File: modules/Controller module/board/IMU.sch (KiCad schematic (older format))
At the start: 9 parts, among them J8 Conn_01x08_Female, U4 MPU-6050

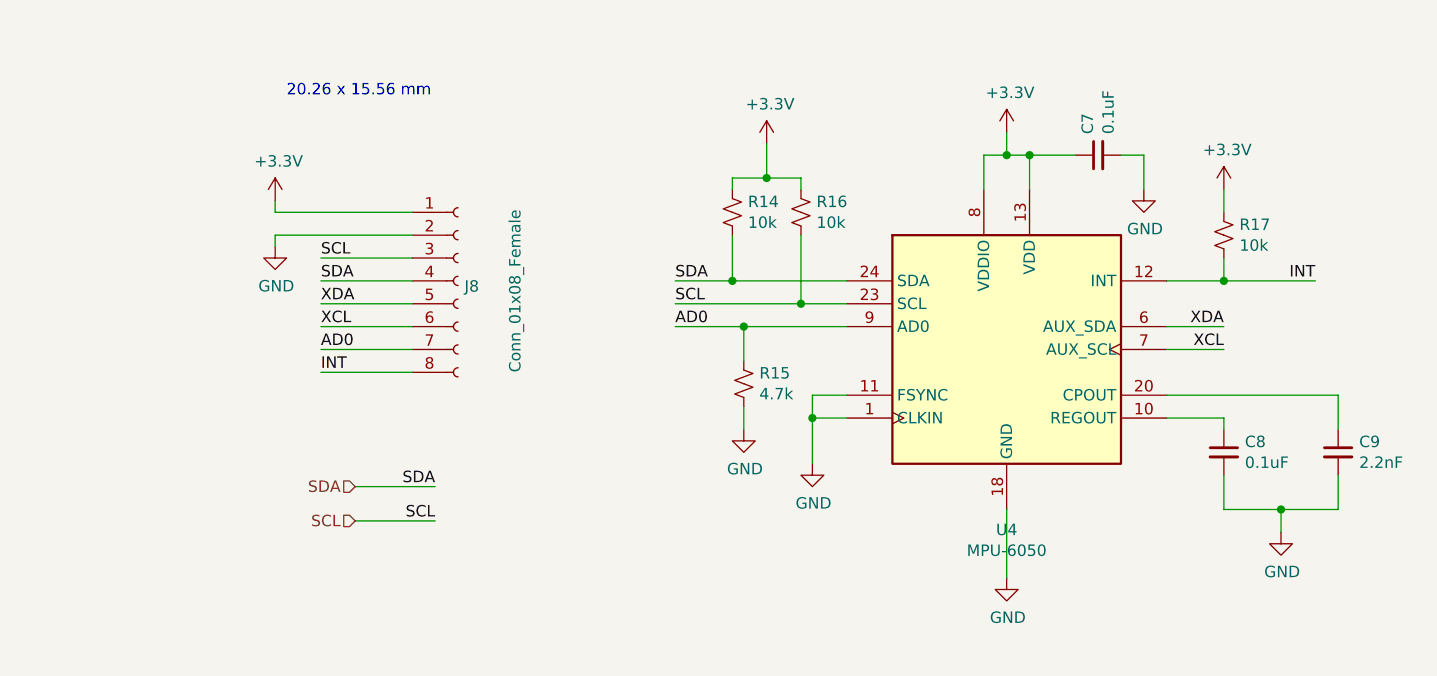
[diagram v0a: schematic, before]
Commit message: Controller module: Schematic and PCB layout
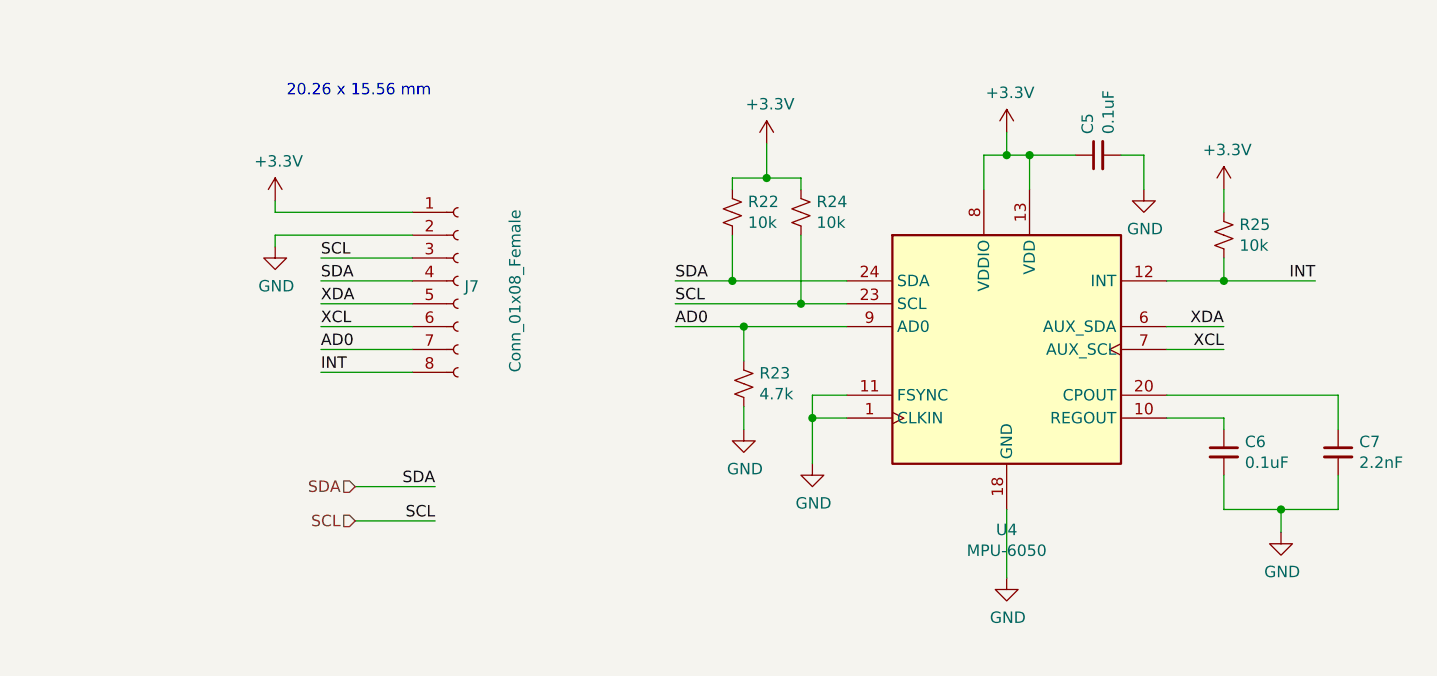
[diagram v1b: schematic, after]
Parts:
- J7: renamed from J8; footprint Connector_PinSocket_2.54mm:PinSocket_1x08_P2.54mm_Vertical -> Board:MPU6050_Breakout
- renumbered C7 to C5, C8 to C6, C9 to C7, R14 to R22, R15 to R23, R16 to R24, R17 to R25
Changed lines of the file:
@@
 $EndDescr
 $Comp
-L Device:R_Small_US R14
+L Device:R_Small_US R22
 U 1 1 61A150D2
 P 5950 2800
-F 0 "R14" H 6018 2846 50  0000 L CNN
+F 0 "R22" H 6018 2846 50  0000 L CNN
 F 1 "10k" H 6018 2755 50  0000 L CNN
 F 2 "Resistor_SMD:R_0805_2012Metric_Pad1.20x1.40mm_HandSolder" H 5950 2800 50  0001 C CNN
@@
 $EndComp
 $Comp
-L Device:R_Small_US R16
+L Device:R_Small_US R24
 U 1 1 61A15DBA
 P 6250 2800
-F 0 "R16" H 6318 2846 50  0000 L CNN
+F 0 "R24" H 6318 2846 50  0000 L CNN
 F 1 "10k" H 6318 2755 50  0000 L CNN
 F 2 "Resistor_SMD:R_0805_2012Metric_Pad1.20x1.40mm_HandSolder" H 6250 2800 50  0001 C CNN
@@
 	6300 3600 6300 3700
 $Comp
-L power:GND #PWR044
+L power:GND #PWR047
 U 1 1 61A173F2
 P 7150 4400
-F 0 "#PWR044" H 7150 4150 50  0001 C CNN
+F 0 "#PWR047" H 7150 4150 50  0001 C CNN
 F 1 "GND" H 7155 4227 50  0000 C CNN
 F 2 "" H 7150 4400 50  0001 C CNN
@@
 	7150 4400 7150 4100
 $Comp
-L Device:C_Small C9
+L Device:C_Small C7
 U 1 1 61A181FF
 P 8600 3850
-F 0 "C9" H 8692 3896 50  0000 L CNN
+F 0 "C7" H 8692 3896 50  0000 L CNN
 F 1 "2.2nF" H 8692 3805 50  0000 L CNN
 F 2 "Capacitor_SMD:C_0805_2012Metric_Pad1.18x1.45mm_HandSolder" H 8600 3850 50  0001 C CNN
@@
 $EndComp
 $Comp
-L Device:C_Small C8
+L Device:C_Small C6
 U 1 1 61A18A43
 P 8100 3850
-F 0 "C8" H 8192 3896 50  0000 L CNN
+F 0 "C6" H 8192 3896 50  0000 L CNN
 F 1 "0.1uF" H 8192 3805 50  0000 L CNN
 F 2 "Capacitor_SMD:C_0805_2012Metric_Pad1.18x1.45mm_HandSolder" H 8100 3850 50  0001 C CNN
@@
 	8350 4100 8600 4100
 $Comp
-L power:GND #PWR040
+L power:GND #PWR043
 U 1 1 61A1AE2E
 P 6000 3750
-F 0 "#PWR040" H 6000 3500 50  0001 C CNN
+F 0 "#PWR043" H 6000 3500 50  0001 C CNN
 F 1 "GND" H 6005 3577 50  0000 C CNN
 F 2 "" H 6000 3750 50  0001 C CNN
@@
 $EndComp
 $Comp
-L power:GND #PWR047
+L power:GND #PWR050
 U 1 1 61A1B162
 P 8350 4200
-F 0 "#PWR047" H 8350 3950 50  0001 C CNN
+F 0 "#PWR050" H 8350 3950 50  0001 C CNN
 F 1 "GND" H 8355 4027 50  0000 C CNN
 F 2 "" H 8350 4200 50  0001 C CNN
@@
 INT
 $Comp
-L power:+3.3V #PWR041
+L power:+3.3V #PWR044
 U 1 1 61A1F691
 P 6100 2500
-F 0 "#PWR041" H 6100 2350 50  0001 C CNN
+F 0 "#PWR044" H 6100 2350 50  0001 C CNN
 F 1 "+3.3V" H 6115 2673 50  0000 C CNN
 F 2 "" H 6100 2500 50  0001 C CNN
@@
 	6000 3300 6450 3300
 $Comp
-L Device:R_Small_US R15
+L Device:R_Small_US R23
 U 1 1 61A2410C
 P 6000 3550
-F 0 "R15" H 6068 3596 50  0000 L CNN
+F 0 "R23" H 6068 3596 50  0000 L CNN
 F 1 "4.7k" H 6068 3505 50  0000 L CNN
 F 2 "Resistor_SMD:R_0805_2012Metric_Pad1.20x1.40mm_HandSolder" H 6000 3550 50  0001 C CNN
@@
 AD0
 $Comp
-L Device:R_Small_US R17
+L Device:R_Small_US R25
 U 1 1 61A254F5
 P 8100 2900
-F 0 "R17" H 8168 2946 50  0000 L CNN
+F 0 "R25" H 8168 2946 50  0000 L CNN
 F 1 "10k" H 8168 2855 50  0000 L CNN
 F 2 "Resistor_SMD:R_0805_2012Metric_Pad1.20x1.40mm_HandSolder" H 8100 2900 50  0001 C CNN
@@
 $EndComp
 $Comp
-L power:+3.3V #PWR046
+L power:+3.3V #PWR049
 U 1 1 61A254FC
 P 8100 2700
-F 0 "#PWR046" H 8100 2550 50  0001 C CNN
+F 0 "#PWR049" H 8100 2550 50  0001 C CNN
 F 1 "+3.3V" H 8115 2873 50  0000 C CNN
 F 2 "" H 8100 2700 50  0001 C CNN
@@
 	8100 2700 8100 2800
 $Comp
-L power:GND #PWR042
+L power:GND #PWR045
 U 1 1 61A2C29B
 P 6300 3900
-F 0 "#PWR042" H 6300 3650 50  0001 C CNN
+F 0 "#PWR045" H 6300 3650 50  0001 C CNN
 F 1 "GND" H 6305 3727 50  0000 C CNN
 F 2 "" H 6300 3900 50  0001 C CNN
@@
 AD0
 $Comp
-L Connector:Conn_01x08_Female J8
+L Connector:Conn_01x08_Female J7
 U 1 1 61A32798
 P 4750 3100
-F 0 "J8" H 4778 3076 50  0000 L CNN
+F 0 "J7" H 4778 3076 50  0000 L CNN
 F 1 "Conn_01x08_Female" V 5000 2700 50  0000 L CNN
-F 2 "Connector_PinSocket_2.54mm:PinSocket_1x08_P2.54mm_Vertical" H 4750 3100 50  0001 C CNN
+F 2 "Board:MPU6050_Breakout" H 4750 3100 50  0001 C CNN
 F 3 "~" H 4750 3100 50  0001 C CNN
 	1    4750 3100
@@
 	3950 2900 3950 2950
 $Comp
-L power:+3.3V #PWR038
+L power:+3.3V #PWR041
 U 1 1 61A36F21
 P 3950 2750
-F 0 "#PWR038" H 3950 2600 50  0001 C CNN
+F 0 "#PWR041" H 3950 2600 50  0001 C CNN
 F 1 "+3.3V" H 3965 2923 50  0000 C CNN
 F 2 "" H 3950 2750 50  0001 C CNN
@@
 $EndComp
 $Comp
-L power:GND #PWR039
+L power:GND #PWR042
 U 1 1 61A37647
 P 3950 2950
-F 0 "#PWR039" H 3950 2700 50  0001 C CNN
+F 0 "#PWR042" H 3950 2700 50  0001 C CNN
 F 1 "GND" H 3955 2777 50  0000 C CNN
 F 2 "" H 3950 2950 50  0001 C CNN
@@
 20.26 x 15.56 mm
 $Comp
-L power:+3.3V #PWR043
+L power:+3.3V #PWR046
 U 1 1 61A16C94
 P 7150 2450
-F 0 "#PWR043" H 7150 2300 50  0001 C CNN
+F 0 "#PWR046" H 7150 2300 50  0001 C CNN
 F 1 "+3.3V" H 7165 2623 50  0000 C CNN
 F 2 "" H 7150 2450 50  0001 C CNN
@@
 $EndComp
 $Comp
-L Device:C_Small C7
+L Device:C_Small C5
 U 1 1 61A3D7BC
 P 7550 2550
-F 0 "C7" H 7642 2596 50  0000 L CNN
+F 0 "C5" H 7642 2596 50  0000 L CNN
 F 1 "0.1uF" H 7642 2505 50  0000 L CNN
 F 2 "Capacitor_SMD:C_0805_2012Metric_Pad1.18x1.45mm_HandSolder" H 7550 2550 50  0001 C CNN
@@
 	6000 3650 6000 3750
 $Comp
-L power:GND #PWR045
+L power:GND #PWR048
 U 1 1 61A3EAA3
 P 7750 2700
-F 0 "#PWR045" H 7750 2450 50  0001 C CNN
+F 0 "#PWR048" H 7750 2450 50  0001 C CNN
 F 1 "GND" H 7755 2527 50  0000 C CNN
 F 2 "" H 7750 2700 50  0001 C CNN

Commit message: Controller module: PCB complete
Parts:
- renumbered R22 to R23, R23 to R24, R24 to R25, R25 to R26
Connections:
- net +3V3: no longer J7.1 (Pin_1)
- new net VCC: J7.1 (Pin_1)
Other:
- moved on the sheet: C5, C6, C7, J7, R23, R24, R25, R26, U4

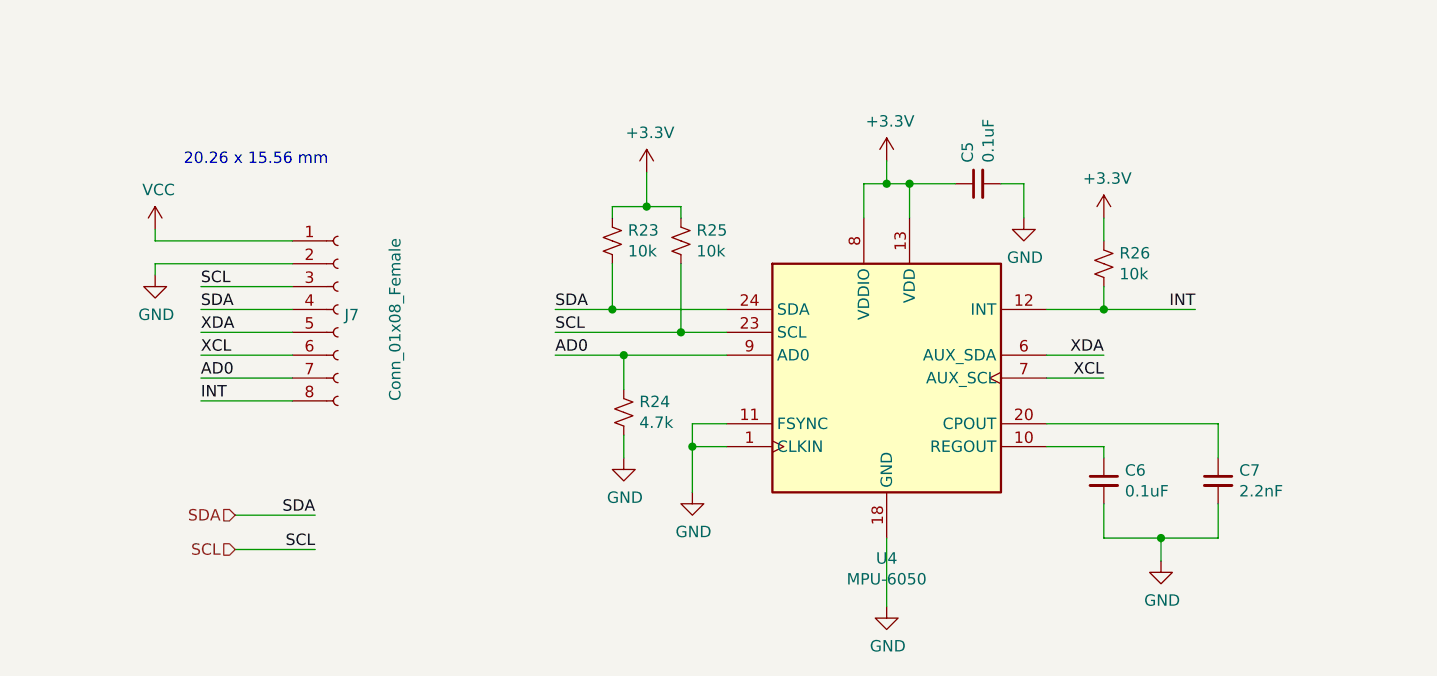
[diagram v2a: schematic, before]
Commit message: PCB: IMU
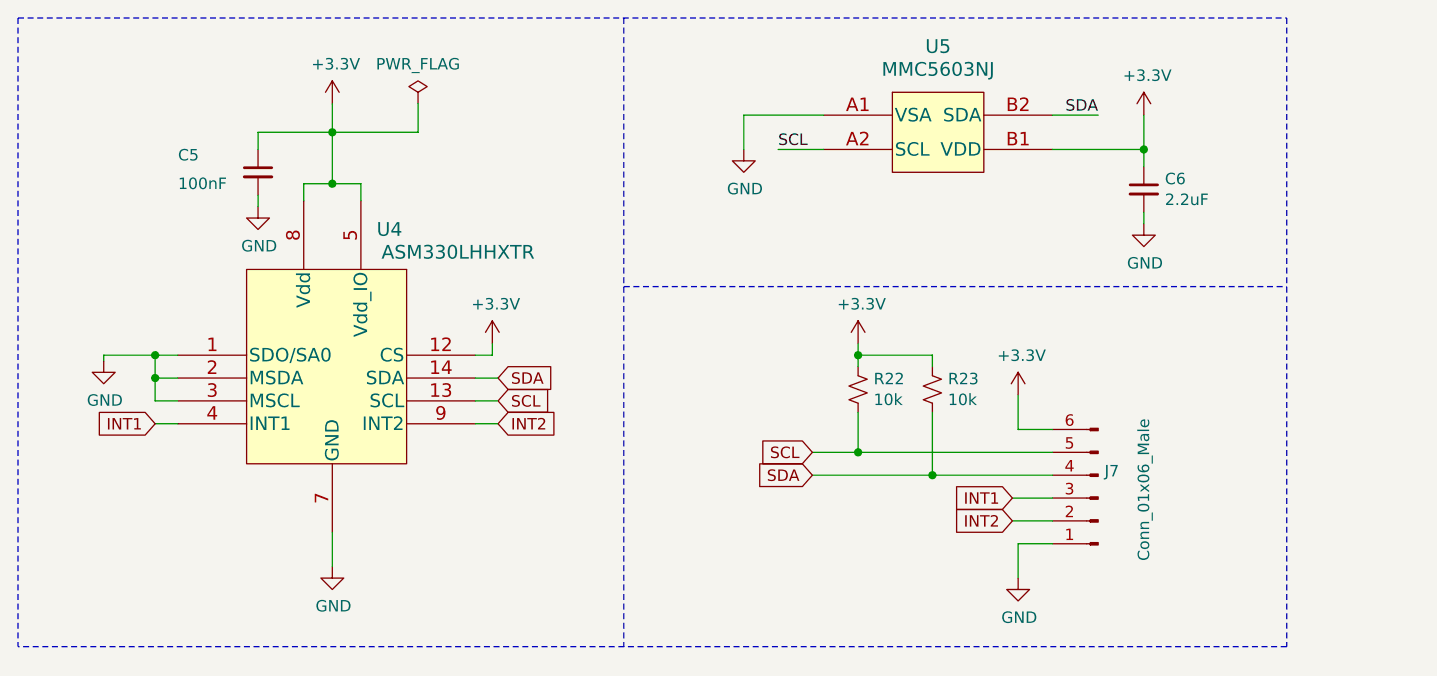
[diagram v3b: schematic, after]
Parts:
- removed C7: 2.2nF, Capacitor_SMD:C_0805_2012Metric_Pad1.18x1.45mm_HandSolder, symbol Device:C_Small
- removed J7: Conn_01x08_Female, Board:MPU6050_Breakout, symbol Connector:Conn_01x08_Female
- removed R24: 4.7k, Resistor_SMD:R_0805_2012Metric_Pad1.20x1.40mm_HandSolder, symbol Device:R_Small_US
- removed R25, R26: 10k, Resistor_SMD:R_0805_2012Metric_Pad1.20x1.40mm_HandSolder, symbol Device:R_Small_US
- removed U4: MPU-6050, Sensor_Motion:InvenSense_QFN-24_4x4mm_P0.5mm, symbol Sensor_Motion:MPU-6050
- added J7: Conn_01x06_Male, Board:SolderWire_1x06_P2.54mm, symbol Connector:Conn_01x06_Male
- added R22: 10k, Resistor_SMD:R_0603_1608Metric_Pad0.98x0.95mm_HandSolder, symbol Device:R_Small_US
- added U4: ASM330LHHXTR, Board:ASM330LHHXTR, symbol ASM330LHHXTR:ASM330LHHXTR
- added U5: MMC5603NJ, Board:MMC5603NJ, symbol MMC5603NJ:MMC5603NJ
- C5: value 0.1uF -> 100nF; footprint Capacitor_SMD:C_0805_2012Metric_Pad1.18x1.45mm_HandSolder -> Capacitor_SMD:C_0603_1608Metric_Pad1.08x0.95mm_HandSolder
- C6: value 0.1uF -> 2.2uF; footprint Capacitor_SMD:C_0805_2012Metric_Pad1.18x1.45mm_HandSolder -> Capacitor_SMD:C_0603_1608Metric_Pad1.08x0.95mm_HandSolder
- R23: footprint Resistor_SMD:R_0805_2012Metric_Pad1.20x1.40mm_HandSolder -> Resistor_SMD:R_0603_1608Metric_Pad0.98x0.95mm_HandSolder
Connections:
- net +3V3: now also C6.1, J7.6 (Pin_6), R22.1, U4.12 (CS), U4.5 (Vdd_IO), U4.8 (Vdd), U5.B1 (VDD)
- net GND: now also J7.1 (Pin_1), U4.1 (SDO/SA0), U4.2 (MSDA), U4.3 (MSCL), U4.7 (GND), U5.A1 (VSA)
- net SCL: now also J7.5 (Pin_5), R22.2, U4.13 (SCL), U5.A2 (SCL)
- net SDA: now also J7.4 (Pin_4), U4.14 (SDA), U5.B2 (SDA)
- new net INT1: J7.3 (Pin_3), U4.4 (INT1)
- new net INT2: J7.2 (Pin_2), U4.9 (INT2)
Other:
- note removed: "20.26 x 15.56 mm"

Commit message: Controller module: Optical Flow Sensor Connector
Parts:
- renumbered C5 to C4, C6 to C5, J7 to J6, R22 to R20, R23 to R21
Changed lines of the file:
@@
 $Descr A4 11693 8268
 encoding utf-8
-Sheet 3 3
+Sheet 3 4
 Title ""
 Date ""
@@
 	4825 3425 4900 3425
 $Comp
-L Device:R_Small_US R22
+L Device:R_Small_US R20
 U 1 1 63B138DD
 P 6500 3575
-F 0 "R22" H 6568 3621 50  0000 L CNN
+F 0 "R20" H 6568 3621 50  0000 L CNN
 F 1 "10k" H 6568 3530 50  0000 L CNN
 F 2 "Resistor_SMD:R_0603_1608Metric_Pad0.98x0.95mm_HandSolder" H 6500 3575 50  0001 C CNN
@@
 $EndComp
 $Comp
-L Device:R_Small_US R23
+L Device:R_Small_US R21
 U 1 1 63B146C8
 P 6825 3575
-F 0 "R23" H 6893 3621 50  0000 L CNN
+F 0 "R21" H 6893 3621 50  0000 L CNN
 F 1 "10k" H 6893 3530 50  0000 L CNN
 F 2 "Resistor_SMD:R_0603_1608Metric_Pad0.98x0.95mm_HandSolder" H 6825 3575 50  0001 C CNN
@@
 SDA
 $Comp
-L Device:C_Small C6
+L Device:C_Small C5
 U 1 1 63B1B7EF
 P 7750 2700
-F 0 "C6" H 7842 2746 50  0000 L CNN
+F 0 "C5" H 7842 2746 50  0000 L CNN
 F 1 "2.2uF" H 7842 2655 50  0000 L CNN
 F 2 "Capacitor_SMD:C_0603_1608Metric_Pad1.08x0.95mm_HandSolder" H 7750 2700 50  0001 C CNN
@@
 	4200 2675 4325 2675
 $Comp
-L Device:C_Small C5
+L Device:C_Small C4
 U 1 1 63B2365E
 P 3875 2625
-F 0 "C5" H 3525 2700 50  0000 L CNN
+F 0 "C4" H 3525 2700 50  0000 L CNN
 F 1 "100nF" H 3525 2575 50  0000 L CNN
 F 2 "Capacitor_SMD:C_0603_1608Metric_Pad1.08x0.95mm_HandSolder" H 3875 2625 50  0001 C CNN
@@
 Connection ~ 6825 3950
 $Comp
-L Connector:Conn_01x06_Male J7
+L Connector:Conn_01x06_Male J6
 U 1 1 63B307C0
 P 7550 4050
-F 0 "J7" H 7522 3932 50  0000 R CNN
+F 0 "J6" H 7522 3932 50  0000 R CNN
 F 1 "Conn_01x06_Male" V 7350 4325 50  0000 R CNN
 F 2 "Board:SolderWire_1x06_P2.54mm" H 7550 4050 50  0001 C CNN
